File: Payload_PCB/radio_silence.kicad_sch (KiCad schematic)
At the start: 6 parts, among them Q1 PMOS, Q12 PMOS, Q2 PMOS

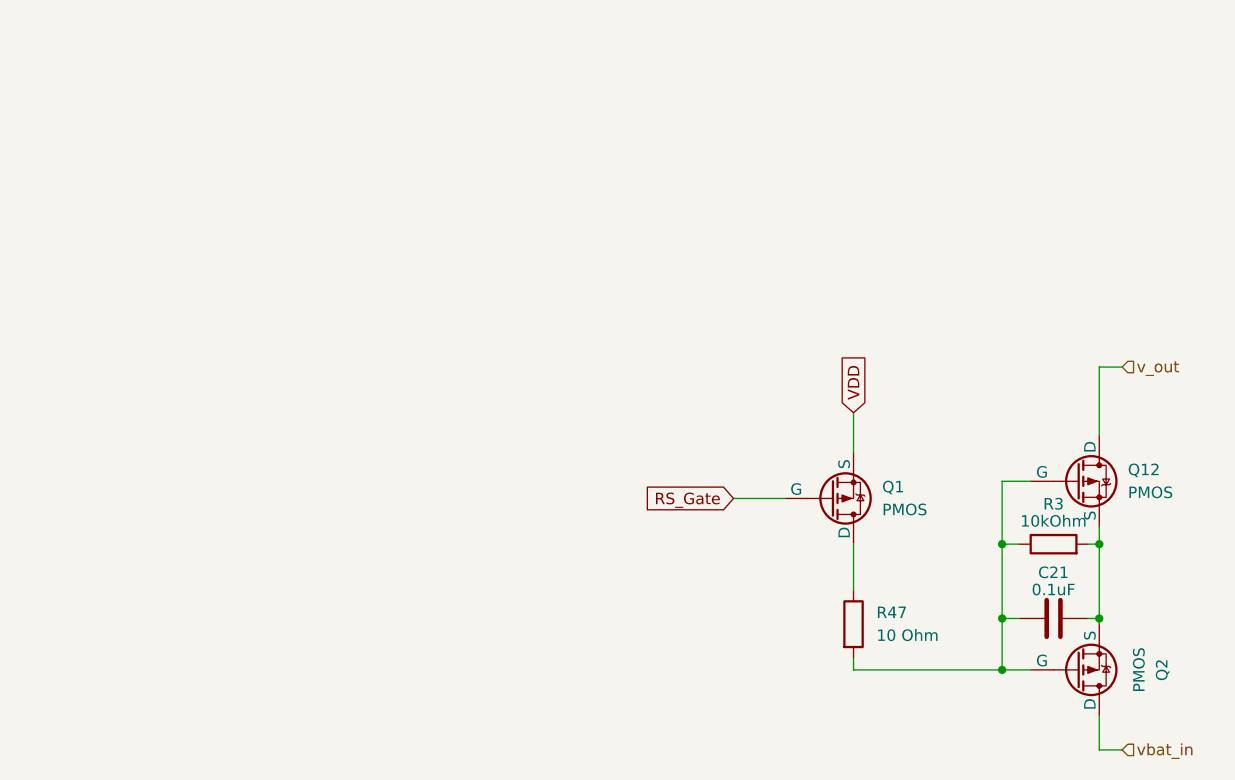
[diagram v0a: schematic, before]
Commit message: Added heating pad, adjustment of page sizes
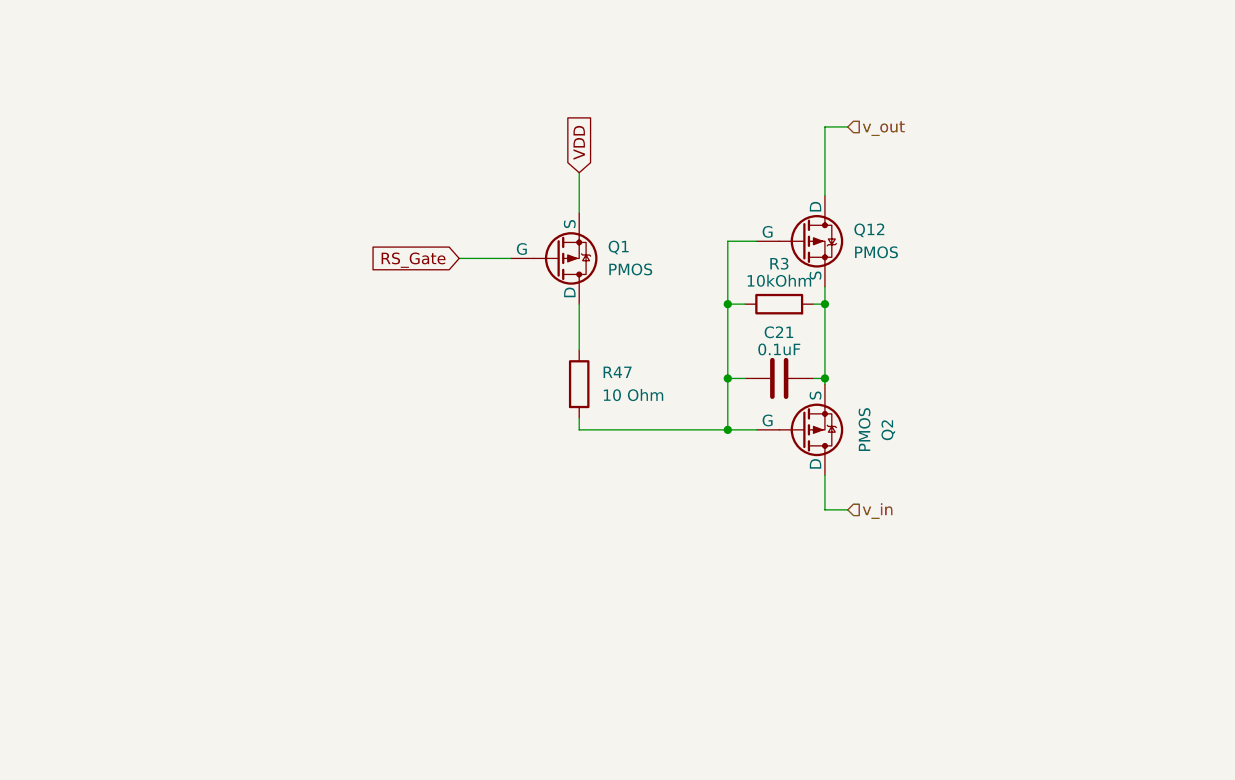
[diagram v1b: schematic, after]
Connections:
- net vbat_in renamed v_in
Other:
- moved on the sheet: C21, Q1, Q12, Q2, R3, R47

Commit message: Added some actual parts
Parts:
- removed Q1, Q12, Q2: PMOS, symbol Simulation_SPICE:PMOS
- added Q14, Q31: SQD50P04-13L_T4GE3, PMOSGSD_TO-252AA_VIS, symbol SQD50P04-13L:SQD50P04-13L_T4GE3
- added Q16: BSH105,235, SOT95P230X110-3N, symbol BSH105_235:BSH105,235
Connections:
- net RS_Gate: now also Q16.1 (GATE)
- net v_in: now also Q14.3 (D)
- net v_out: now also Q31.3 (D)
- net at C21.2, R3.1, R47.2: now also Q14.1 (G), Q31.1 (G)
- net at C21.1, R3.2: now also Q14.2 (S), Q31.2 (S)
- net at R47.1: now also Q16.3 (DRAIN)
- new net GND: Q16.2 (SOURCE)
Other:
- company: (none) -> SpaceTeam Aachen
- title: (none) -> Radio Silence Switch
- moved on the sheet: C21, R3, R47

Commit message: some new parts
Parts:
- Q14, Q31: footprint PMOSGSD_TO-252AA_VIS -> footprints:PMOSGSD_TO-252AA_VIS
- Q16: footprint SOT95P230X110-3N -> footprints:SOT95P230X110-3N
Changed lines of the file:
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@@
       (effects (font (size 1.524 1.524)) (justify left))
     )
-    (property "Footprint" "PMOSGSD_TO-252AA_VIS" (at 106.68 50.8 0)
+    (property "Footprint" "footprints:PMOSGSD_TO-252AA_VIS" (at 106.68 50.8 0)
       (effects (font (size 1.27 1.27) italic) hide)
     )
@@
       (effects (font (size 1.524 1.524)) (justify left))
     )
-    (property "Footprint" "PMOSGSD_TO-252AA_VIS" (at 106.68 78.105 0)
+    (property "Footprint" "footprints:PMOSGSD_TO-252AA_VIS" (at 106.68 78.105 0)
       (effects (font (size 1.27 1.27) italic) hide)
     )
@@
       (effects (font (size 1.27 1.27)))
     )
-    (property "Footprint" "SOT95P230X110-3N" (at 83.185 152.07 0)
+    (property "Footprint" "footprints:SOT95P230X110-3N" (at 83.185 152.07 0)
       (effects (font (size 1.27 1.27)) (justify left top) hide)
     )

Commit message: Todo notes after review
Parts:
- added R66: 100 kOhm, symbol Device:R
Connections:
- net GND: now also R66.2
- net RS_Gate: now also R66.1
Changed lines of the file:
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@@
   (junction (at 114.3 62.23) (diameter 0) (color 0 0 0 0)
   )
+  (junction (at 40.64 57.15) (diameter 0) (color 0 0 0 0)
+  )
   (junction (at 103.505 78.105) (diameter 0) (color 0 0 0 0)
   )
+  (junction (at 53.975 74.295) (diameter 0) (color 0 0 0 0)
+  )
   (junction (at 103.505 62.23) (diameter 0) (color 0 0 0 0)
   )
@@
     (stroke (width 0) (type default))
   )
+  (wire (pts (xy 40.64 57.15) (xy 53.975 57.15))
+    (stroke (width 0) (type default))
+  )
   (wire (pts (xy 103.505 62.23) (xy 103.505 69.85))
     (stroke (width 0) (type default))
   )
+  (wire (pts (xy 53.975 78.74) (xy 53.975 74.295))
+    (stroke (width 0) (type default))
+  )
   (wire (pts (xy 114.3 83.185) (xy 114.3 84.455))
     (stroke (width 0) (type default))
@@
     (stroke (width 0) (type default))
   )
+  (wire (pts (xy 36.83 57.15) (xy 40.64 57.15))
+    (stroke (width 0) (type default))
+  )
+  (wire (pts (xy 53.975 74.295) (xy 53.975 59.69))
+    (stroke (width 0) (type default))
+  )
   (wire (pts (xy 106.68 50.8) (xy 103.505 50.8))
     (stroke (width 0) (type default))
@@
     (stroke (width 0) (type default))
   )
+  (wire (pts (xy 40.64 74.295) (xy 53.975 74.295))
+    (stroke (width 0) (type default))
+  )
   (wire (pts (xy 114.3 84.455) (xy 116.84 84.455))
     (stroke (width 0) (type default))
   )
+  (wire (pts (xy 40.64 57.15) (xy 40.64 62.23))
+    (stroke (width 0) (type default))
+  )
   (wire (pts (xy 114.3 41.91) (xy 116.84 41.91))
     (stroke (width 0) (type default))
@@
     (stroke (width 0) (type default))
   )
-  (global_label "RS_Gate" (shape input) (at 53.975 57.15 180) (fields_autoplaced)
+  (wire (pts (xy 40.64 69.85) (xy 40.64 74.295))
+    (stroke (width 0) (type default))
+  )
+  (global_label "RS_Gate" (shape input) (at 36.83 57.15 180) (fields_autoplaced)
     (effects (font (size 1.27 1.27)) (justify right))
-    (property "Intersheetrefs" "${INTERSHEET_REFS}" (at 43.3094 57.15 0)
+    (property "Intersheetrefs" "${INTERSHEET_REFS}" (at 26.1644 57.15 0)
       (effects (font (size 1.27 1.27)) (justify right) hide)
     )
   )
-  (global_label "GND" (shape input) (at 53.975 59.69 180) (fields_autoplaced)
+  (global_label "GND" (shape input) (at 53.975 78.74 270) (fields_autoplaced)
     (effects (font (size 1.27 1.27)) (justify right))
-    (property "Intersheetrefs" "${INTERSHEET_REFS}" (at 47.1193 59.69 0)
+    (property "Intersheetrefs" "${INTERSHEET_REFS}" (at 53.975 85.5957 90)
       (effects (font (size 1.27 1.27)) (justify right) hide)
     )
@@
         )
       )
+    )
+  )
+  (symbol (lib_id "Device:R") (at 40.64 66.04 0) (unit 1)
+    (in_bom yes) (on_board yes) (dnp no) (fields_autoplaced)
+    (property "Reference" "R66" (at 43.18 64.77 0)
+      (effects (font (size 1.27 1.27)) (justify left))
+    )
+    (property "Value" "100 kOhm" (at 43.18 67.31 0)
+      (effects (font (size 1.27 1.27)) (justify left))
+    )
+    (property "Footprint" "" (at 38.862 66.04 90)
+      (effects (font (size 1.27 1.27)) hide)
+    )
+    (property "Datasheet" "~" (at 40.64 66.04 0)
+      (effects (font (size 1.27 1.27)) hide)
+    )
+    (pin "1")
+    (pin "2")
+    (instances
+      (project "Payload_PCB"
+        (path "/5c4f9a68-5778-4223-b18a-2e31db8d7d40/a5d6e803-a43d-4b6f-b631-9dac7ff20cfd/230fdfe9-a3f7-4a15-ad2e-fce3439d80d7"
+          (reference "R66") (unit 1)
+        )
+        (path "/5c4f9a68-5778-4223-b18a-2e31db8d7d40/a5d6e803-a43d-4b6f-b631-9dac7ff20cfd/d3c6e6f5-d724-48e9-8547-c8822d927132"
+          (reference "R46") (unit 1)
+        )
+        (path "/5c4f9a68-5778-4223-b18a-2e31db8d7d40/722fc623-9945-41d5-bc31-e6d0e92574b1/230fdfe9-a3f7-4a15-ad2e-fce3439d80d7"
+          (reference "R67") (unit 1)
+        )
+        (path "/5c4f9a68-5778-4223-b18a-2e31db8d7d40/722fc623-9945-41d5-bc31-e6d0e92574b1/d3c6e6f5-d724-48e9-8547-c8822d927132"
+          (reference "R68") (unit 1)
+        )
+      )
